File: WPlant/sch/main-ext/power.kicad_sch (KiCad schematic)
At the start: 45 parts, among them J2 Battery, J3 Balance, J4 DE9_Receptacle, U2 AP64352SP-13, U3 AP64352SP-13, U4 AP64352SP-13, U6 AP2204R-5.0

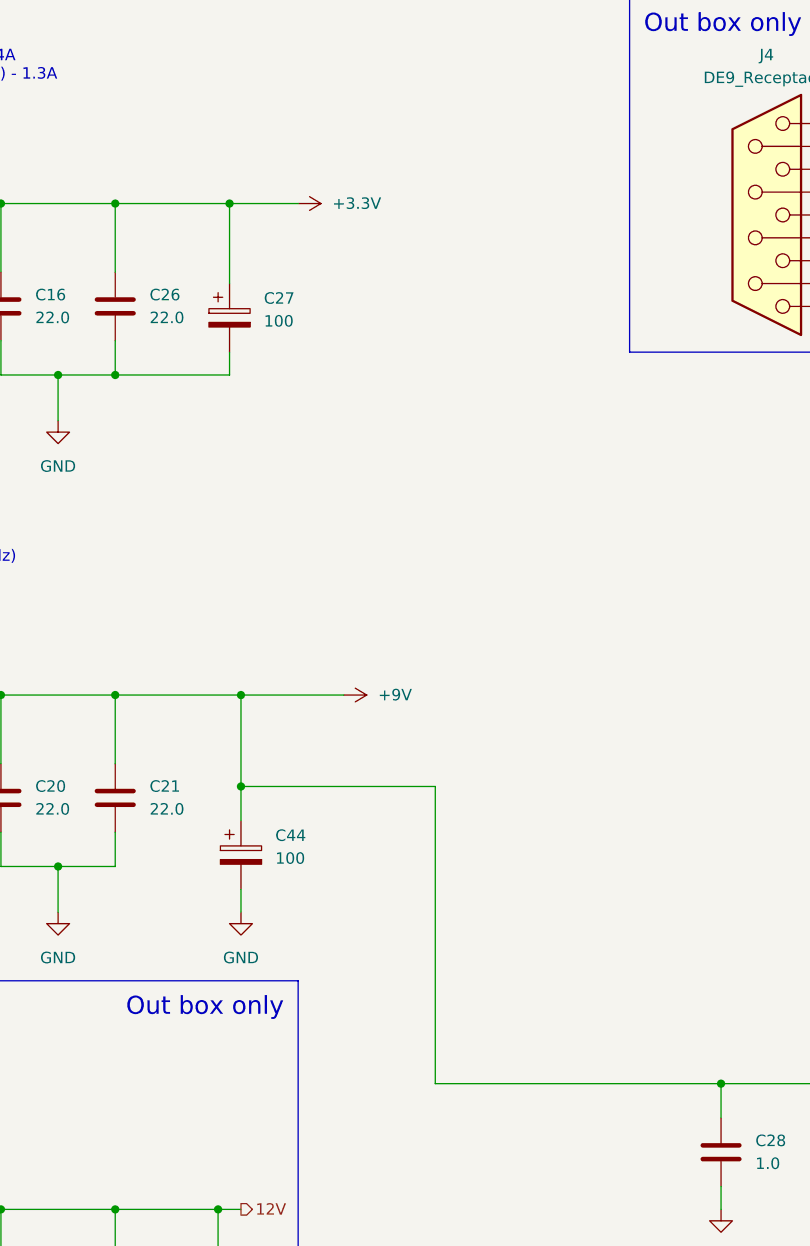
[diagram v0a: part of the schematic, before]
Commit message: Added jumpers to power lines for Main-* schematics
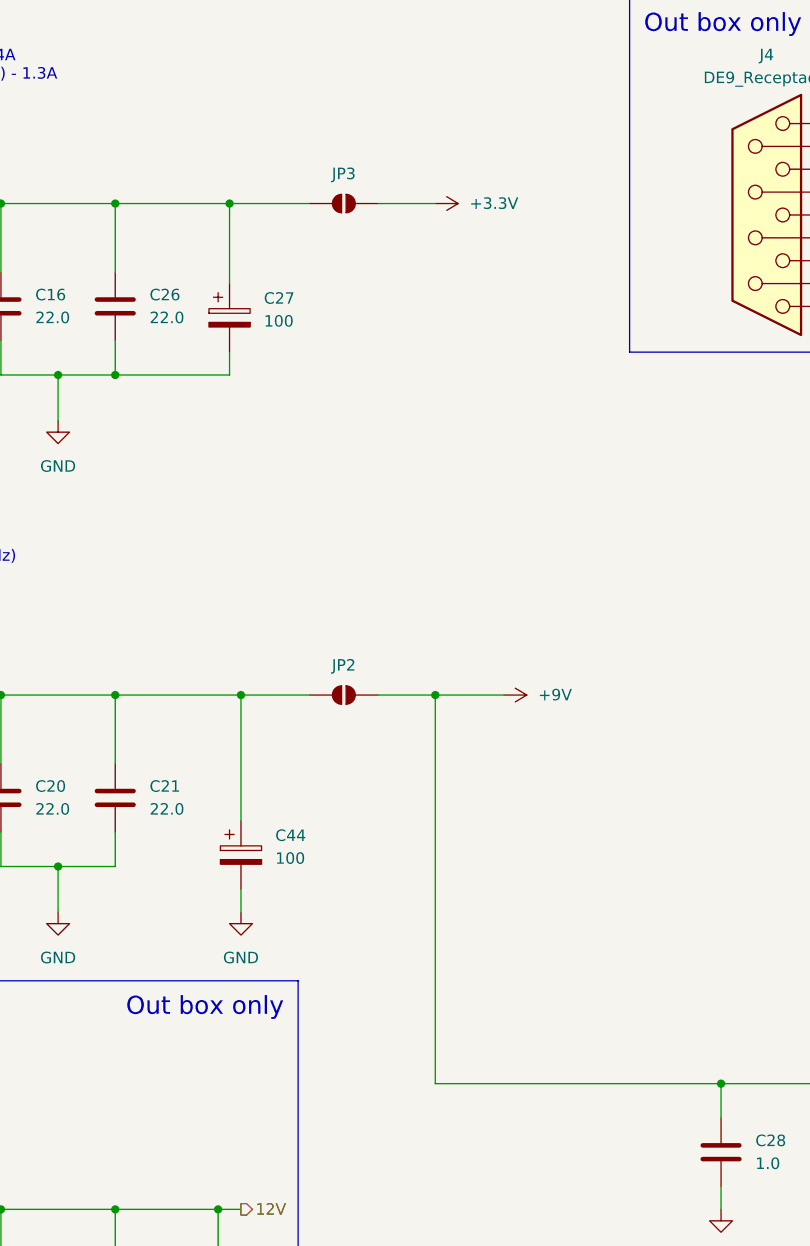
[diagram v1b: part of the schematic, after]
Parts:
- added JP2, JP3: SolderJumper_2_Open, Jumper:SolderJumper-2_P1.3mm_Open_RoundedPad1.0x1.5mm, symbol Jumper:SolderJumper_2_Open
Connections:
- net +3.3V: now also JP3.2 (B); no longer C16.2, C25.2, C26.2, C27.1, L3.2, R17.1
- net +9V: now also JP2.2 (B); no longer C19.2, C20.2, C21.2, C44.1, L2.2, R14.1
- new net: C16.2, C25.2, C26.2, C27.1, JP3.1 (A), L3.2, R17.1
- new net: C19.2, C20.2, C21.2, C44.1, JP2.1 (A), L2.2, R14.1
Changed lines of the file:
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@@
 	)
 	(junction
+		(at 177.8 96.52)
+		(diameter 0)
+		(color 0 0 0 0)
+	)
+	(junction
 		(at 142.24 172.72)
 		(diameter 0)
@@
 	)
 	(junction
-		(at 156.21 106.68)
-		(diameter 0)
-		(color 0 0 0 0)
-	)
-	(junction
 		(at 107.95 153.67)
 		(diameter 0)
@@
 	(wire
 		(pts
-			(xy 156.21 96.52) (xy 156.21 106.68)
+			(xy 156.21 96.52) (xy 156.21 110.49)
 		)
 		(stroke
@@
 	(wire
 		(pts
-			(xy 177.8 139.7) (xy 177.8 106.68)
-		)
-		(stroke
-			(width 0)
-			(type default)
-		)
-	)
-	(wire
-		(pts
 			(xy 246.38 26.67) (xy 246.38 30.48)
 		)
@@
 	(wire
 		(pts
+			(xy 177.8 96.52) (xy 185.42 96.52)
+		)
+		(stroke
+			(width 0)
+			(type default)
+		)
+	)
+	(wire
+		(pts
 			(xy 118.11 109.22) (xy 107.95 109.22)
 		)
@@
 	(wire
 		(pts
+			(xy 171.45 41.91) (xy 177.8 41.91)
+		)
+		(stroke
+			(width 0)
+			(type default)
+		)
+	)
+	(wire
+		(pts
 			(xy 222.25 50.8) (xy 224.79 50.8)
 		)
@@
 	(wire
 		(pts
-			(xy 156.21 106.68) (xy 156.21 110.49)
-		)
-		(stroke
-			(width 0)
-			(type default)
-		)
-	)
-	(wire
-		(pts
 			(xy 107.95 109.22) (xy 107.95 110.49)
 		)
@@
 	(wire
 		(pts
-			(xy 154.94 41.91) (xy 162.56 41.91)
+			(xy 154.94 41.91) (xy 163.83 41.91)
 		)
 		(stroke
@@
 	(wire
 		(pts
-			(xy 156.21 96.52) (xy 167.64 96.52)
+			(xy 156.21 96.52) (xy 163.83 96.52)
 		)
 		(stroke
@@
 	(wire
 		(pts
-			(xy 50.8 161.29) (xy 58.42 161.29)
+			(xy 177.8 96.52) (xy 177.8 139.7)
 		)
 		(stroke
@@
 	(wire
 		(pts
-			(xy 222.25 33.02) (xy 224.79 33.02)
+			(xy 50.8 161.29) (xy 58.42 161.29)
 		)
 		(stroke
@@
 	(wire
 		(pts
-			(xy 107.95 41.91) (xy 118.11 41.91)
+			(xy 222.25 33.02) (xy 224.79 33.02)
 		)
 		(stroke
@@
 	(wire
 		(pts
-			(xy 107.95 53.34) (xy 107.95 54.61)
+			(xy 107.95 41.91) (xy 118.11 41.91)
 		)
 		(stroke
@@
 	(wire
 		(pts
-			(xy 73.66 77.47) (xy 85.09 77.47)
+			(xy 107.95 53.34) (xy 107.95 54.61)
 		)
 		(stroke
@@
 	(wire
 		(pts
-			(xy 156.21 106.68) (xy 177.8 106.68)
+			(xy 73.66 77.47) (xy 85.09 77.47)
 		)
 		(stroke
@@
 	(wire
 		(pts
+			(xy 171.45 96.52) (xy 177.8 96.52)
+		)
+		(stroke
+			(width 0)
+			(type default)
+		)
+	)
+	(wire
+		(pts
 			(xy 50.8 59.69) (xy 50.8 63.5)
 		)
@@
 	(symbol
 		(lib_id "power:+3.3V")
-		(at 162.56 41.91 270)
+		(at 177.8 41.91 270)
 		(unit 1)
 		(exclude_from_sim no)
@@
 		(fields_autoplaced yes)
 		(property "Reference" "#PWR040"
-			(at 158.75 41.91 0)
+			(at 173.99 41.91 0)
 			(effects
 				(font
@@
 		)
 		(property "Value" "+3.3V"
-			(at 166.37 41.9099 90)
+			(at 181.61 41.9099 90)
 			(effects
 				(font
@@
 		)
 		(property "Footprint" ""
-			(at 162.56 41.91 0)
+			(at 177.8 41.91 0)
 			(effects
 				(font
@@
 		)
 		(property "Datasheet" ""
-			(at 162.56 41.91 0)
+			(at 177.8 41.91 0)
 			(effects
 				(font
@@
 		)
 		(property "Description" "Power symbol creates a global label with name \"+3.3V\""
-			(at 162.56 41.91 0)
+			(at 177.8 41.91 0)
 			(effects
 				(font
@@
 	)
 	(symbol
+		(lib_id "Jumper:SolderJumper_2_Open")
+		(at 167.64 41.91 0)
+		(unit 1)
+		(exclude_from_sim yes)
+		(in_bom no)
+		(on_board yes)
+		(dnp no)
+		(property "Reference" "JP3"
+			(at 167.64 38.608 0)
+			(effects
+				(font
+					(size 1.27 1.27)
+				)
+			)
+		)
+		(property "Value" "SolderJumper_2_Open"
+			(at 167.64 38.1 0)
+			(effects
+				(font
+					(size 1.27 1.27)
+				)
+				(hide yes)
+			)
+		)
+		(property "Footprint" "Jumper:SolderJumper-2_P1.3mm_Open_RoundedPad1.0x1.5mm"
+			(at 167.64 41.91 0)
+			(effects
+				(font
+					(size 1.27 1.27)
+				)
+				(hide yes)
+			)
+		)
+		(property "Datasheet" "~"
+			(at 167.64 41.91 0)
+			(effects
+				(font
+					(size 1.27 1.27)
+				)
+				(hide yes)
+			)
+		)
+		(property "Description" "Solder Jumper, 2-pole, open"
+			(at 167.64 41.91 0)
+			(effects
+				(font
+					(size 1.27 1.27)
+				)
+				(hide yes)
+			)
+		)
+		(pin "2"
+		)
+		(pin "1"
+		)
+		(instances
+			(project "main-ext"
+				(path "/71bd3f7f-463d-4a2c-bec7-ca56c2fe6cec/e5010fd4-921a-4703-b472-3554db39dd22"
+					(reference "JP3")
+					(unit 1)
+				)
+			)
+		)
+	)
+	(symbol
 		(lib_id "power:GND")
 		(at 38.1 114.3 0)
@@
 	)
 	(symbol
+		(lib_id "Jumper:SolderJumper_2_Open")
+		(at 167.64 96.52 0)
+		(unit 1)
+		(exclude_from_sim yes)
+		(in_bom no)
+		(on_board yes)
+		(dnp no)
+		(property "Reference" "JP2"
+			(at 167.64 93.218 0)
+			(effects
+				(font
+					(size 1.27 1.27)
+				)
+			)
+		)
+		(property "Value" "SolderJumper_2_Open"
+			(at 167.64 92.71 0)
+			(effects
+				(font
+					(size 1.27 1.27)
+				)
+				(hide yes)
+			)
+		)
+		(property "Footprint" "Jumper:SolderJumper-2_P1.3mm_Open_RoundedPad1.0x1.5mm"
+			(at 167.64 96.52 0)
+			(effects
+				(font
+					(size 1.27 1.27)
+				)
+				(hide yes)
+			)
+		)
+		(property "Datasheet" "~"
+			(at 167.64 96.52 0)
+			(effects
+				(font
+					(size 1.27 1.27)
+				)
+				(hide yes)
+			)
+		)
+		(property "Description" "Solder Jumper, 2-pole, open"
+			(at 167.64 96.52 0)
+			(effects
+				(font
+					(size 1.27 1.27)
+				)
+				(hide yes)
+			)
+		)
+		(pin "2"
+		)
+		(pin "1"
+		)
+		(instances
+			(project ""
+				(path "/71bd3f7f-463d-4a2c-bec7-ca56c2fe6cec/e5010fd4-921a-4703-b472-3554db39dd22"
+					(reference "JP2")
+					(unit 1)
+				)
+			)
+		)
+	)
+	(symbol
 		(lib_id "Device:C")
 		(at 129.54 53.34 180)
@@
 	(symbol
 		(lib_id "power:+9V")
-		(at 167.64 96.52 270)
+		(at 185.42 96.52 270)
 		(unit 1)
 		(exclude_from_sim no)
@@
 		(fields_autoplaced yes)
 		(property "Reference" "#PWR063"
-			(at 163.83 96.52 0)
+			(at 181.61 96.52 0)
 			(effects
 				(font
@@
 		)
 		(property "Value" "+9V"
-			(at 171.45 96.5199 90)
+			(at 189.23 96.5199 90)
 			(effects
 				(font
@@
 		)
 		(property "Footprint" ""
-			(at 167.64 96.52 0)
+			(at 185.42 96.52 0)
 			(effects
 				(font
@@
 		)
 		(property "Datasheet" ""
-			(at 167.64 96.52 0)
+			(at 185.42 96.52 0)
 			(effects
 				(font
@@
 		)
 		(property "Description" "Power symbol creates a global label with name \"+9V\""
-			(at 167.64 96.52 0)
+			(at 185.42 96.52 0)
 			(effects
 				(font

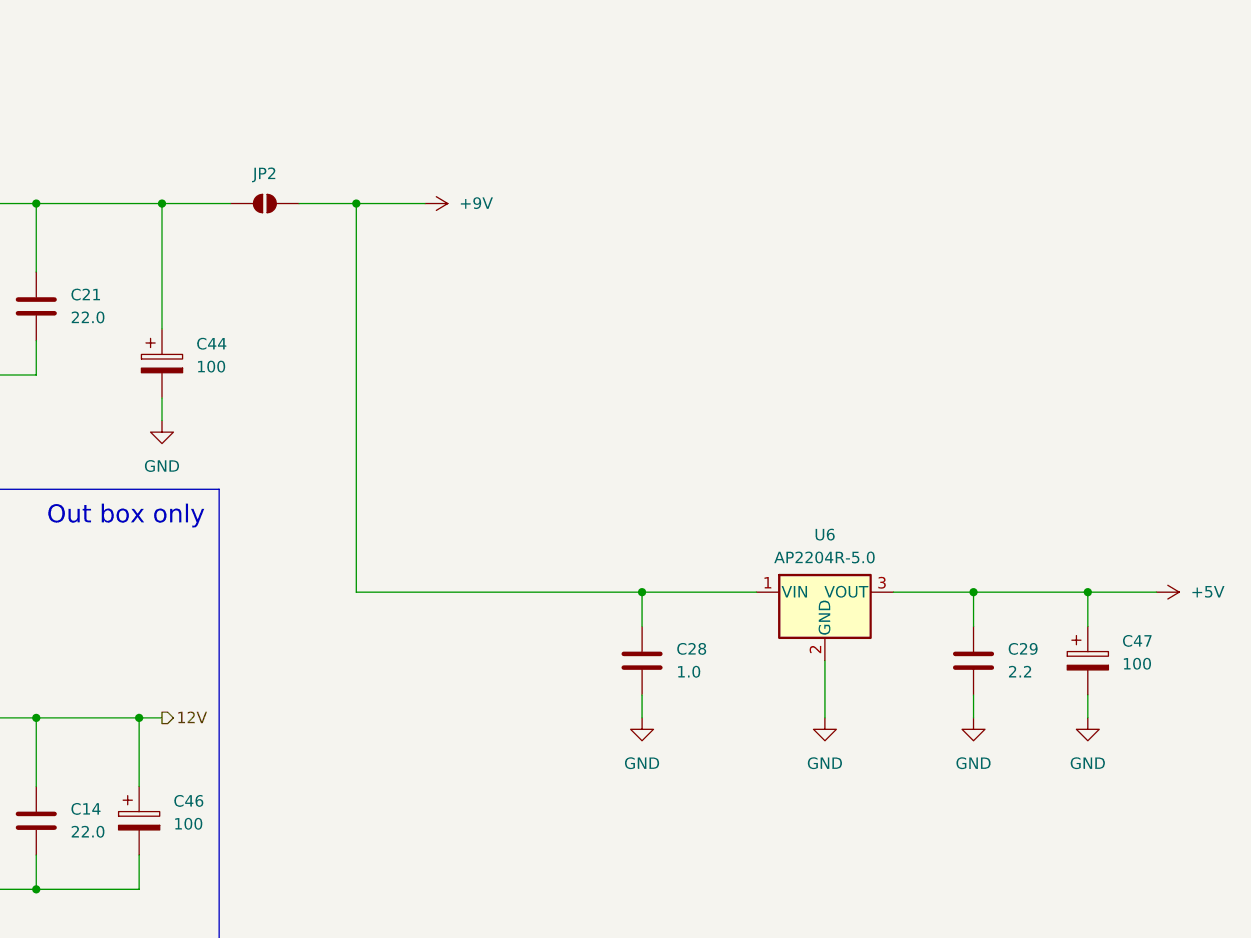
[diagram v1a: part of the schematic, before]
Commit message: Added more jumpers to power lines for Main-* schematics
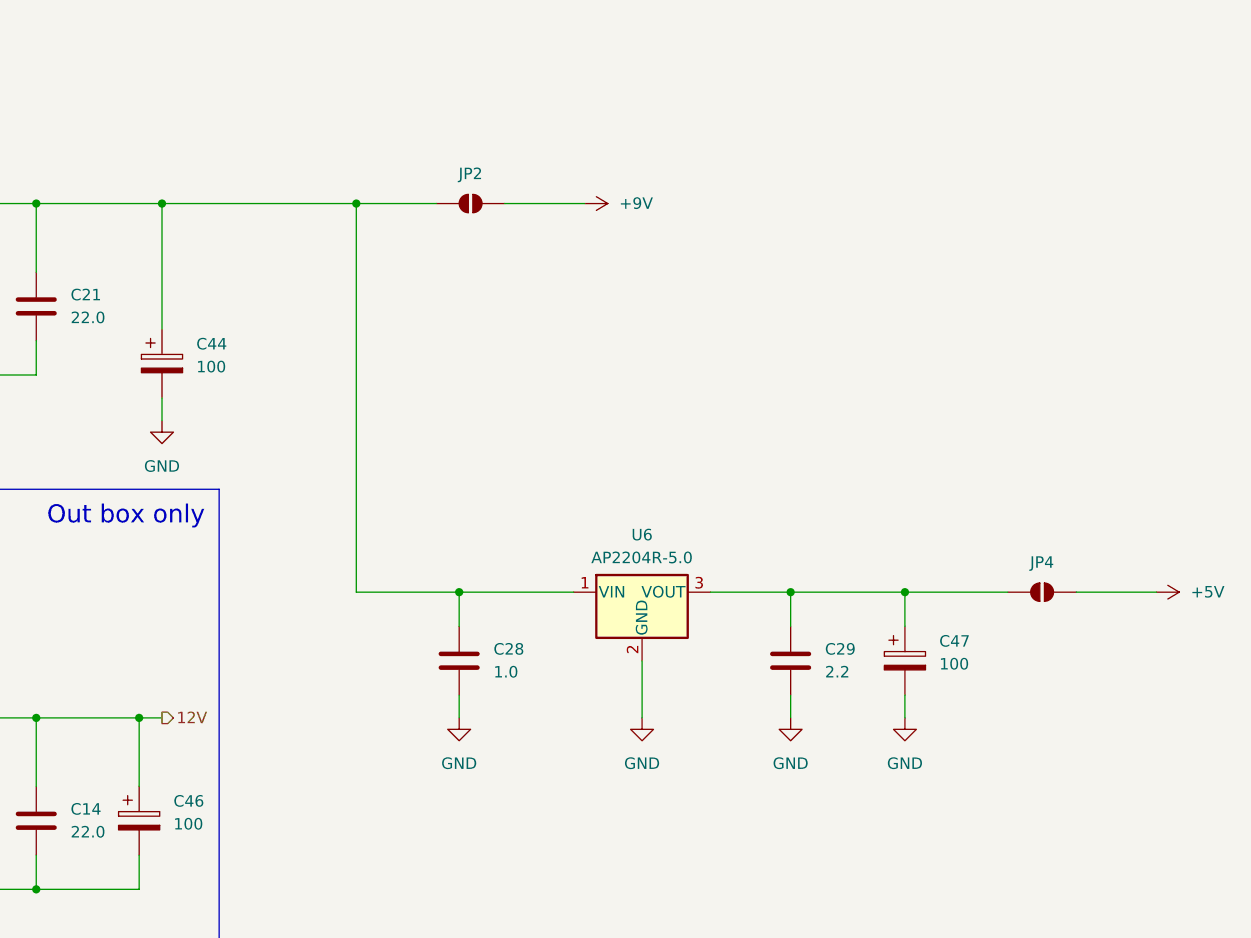
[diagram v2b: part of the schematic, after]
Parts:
- added JP4: SolderJumper_2_Open, Jumper:SolderJumper-2_P1.3mm_Open_RoundedPad1.0x1.5mm, symbol Jumper:SolderJumper_2_Open
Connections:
- net +5V: now also JP4.2 (B); no longer C29.2, C47.1, U6.3 (VOUT)
- net +9V: no longer C28.2, U6.1 (VIN)
- net at C19.2, C20.2, C21.2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: now also C28.2, U6.1 (VIN)
- new net: C29.2, C47.1, JP4.1 (A), U6.3 (VOUT)
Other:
- moved on the sheet: C28, C29, C47, JP2, U6

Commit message: Route of MainInt PCB done
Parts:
- C13, C14, C16, C20, C21, C26: footprint Capacitor_SMD:C_1206_3216Metric_Pad1.33x1.80mm_HandSolder -> Capacitor_SMD:C_1210_3225Metric_Pad1.33x2.70mm_HandSolder
- U2, U3, U4: footprint easyeda2kicad:SO-8_L4.9-W3.9-P1.27-LS6.0-BL-EP -> locals:SO-8_L4.9-W3.9-P1.27-LS6.0-BL-EP
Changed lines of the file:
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@@
 			)
 		)
-		(property "Footprint" "Capacitor_SMD:C_1206_3216Metric_Pad1.33x1.80mm_HandSolder"
+		(property "Footprint" "Capacitor_SMD:C_1210_3225Metric_Pad1.33x2.70mm_HandSolder"
 			(at 141.2748 104.14 0)
 			(effects
@@
 			)
 		)
-		(property "Footprint" "Capacitor_SMD:C_1206_3216Metric_Pad1.33x1.80mm_HandSolder"
+		(property "Footprint" "Capacitor_SMD:C_1210_3225Metric_Pad1.33x2.70mm_HandSolder"
 			(at 128.5748 161.29 0)
 			(effects
@@
 			)
 		)
-		(property "Footprint" "easyeda2kicad:SO-8_L4.9-W3.9-P1.27-LS6.0-BL-EP"
+		(property "Footprint" "locals:SO-8_L4.9-W3.9-P1.27-LS6.0-BL-EP"
 			(at 69.85 111.76 0)
 			(effects
@@
 			)
 		)
-		(property "Footprint" "easyeda2kicad:SO-8_L4.9-W3.9-P1.27-LS6.0-BL-EP"
+		(property "Footprint" "locals:SO-8_L4.9-W3.9-P1.27-LS6.0-BL-EP"
 			(at 69.85 57.15 0)
 			(effects
@@
 			)
 		)
-		(property "Footprint" "Capacitor_SMD:C_1206_3216Metric_Pad1.33x1.80mm_HandSolder"
+		(property "Footprint" "Capacitor_SMD:C_1210_3225Metric_Pad1.33x2.70mm_HandSolder"
 			(at 141.2748 49.53 0)
 			(effects
@@
 			)
 		)
-		(property "Footprint" "easyeda2kicad:SO-8_L4.9-W3.9-P1.27-LS6.0-BL-EP"
+		(property "Footprint" "locals:SO-8_L4.9-W3.9-P1.27-LS6.0-BL-EP"
 			(at 69.85 168.91 0)
 			(effects
@@
 			)
 		)
-		(property "Footprint" "Capacitor_SMD:C_1206_3216Metric_Pad1.33x1.80mm_HandSolder"
+		(property "Footprint" "Capacitor_SMD:C_1210_3225Metric_Pad1.33x2.70mm_HandSolder"
 			(at 128.5748 104.14 0)
 			(effects
@@
 			)
 		)
-		(property "Footprint" "Capacitor_SMD:C_1206_3216Metric_Pad1.33x1.80mm_HandSolder"
+		(property "Footprint" "Capacitor_SMD:C_1210_3225Metric_Pad1.33x2.70mm_HandSolder"
 			(at 128.5748 49.53 0)
 			(effects
@@
 			)
 		)
-		(property "Footprint" "Capacitor_SMD:C_1206_3216Metric_Pad1.33x1.80mm_HandSolder"
+		(property "Footprint" "Capacitor_SMD:C_1210_3225Metric_Pad1.33x2.70mm_HandSolder"
 			(at 141.2748 161.29 0)
 			(effects
